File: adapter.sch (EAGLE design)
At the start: 28 parts, among them Q1 BS170, Q2 BS170, Q3 BS170, Q4 BS170, X2 KUSBVX

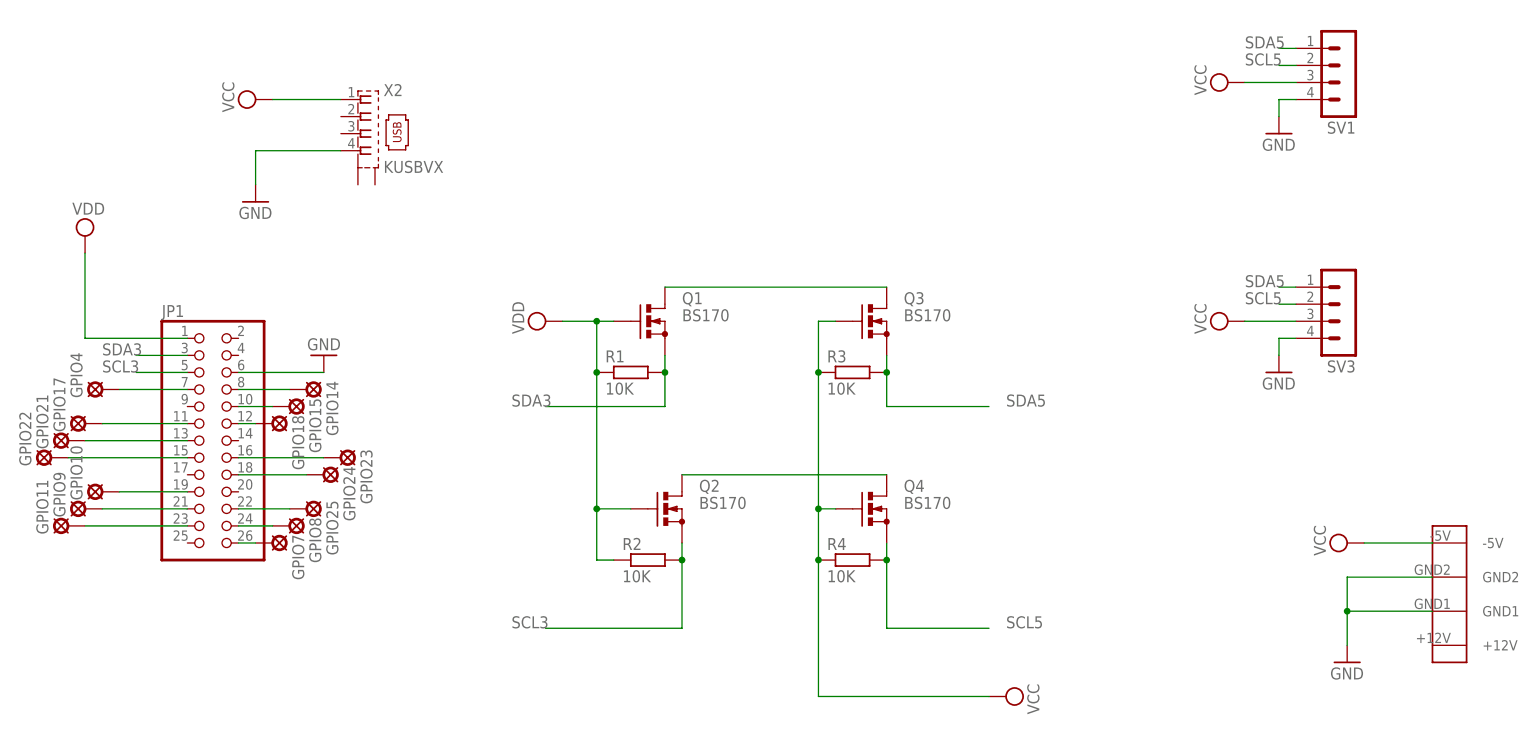
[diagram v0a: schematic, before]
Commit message: Redesign (INT-Leitung und breitere Leitung für Spannungsversorgung)
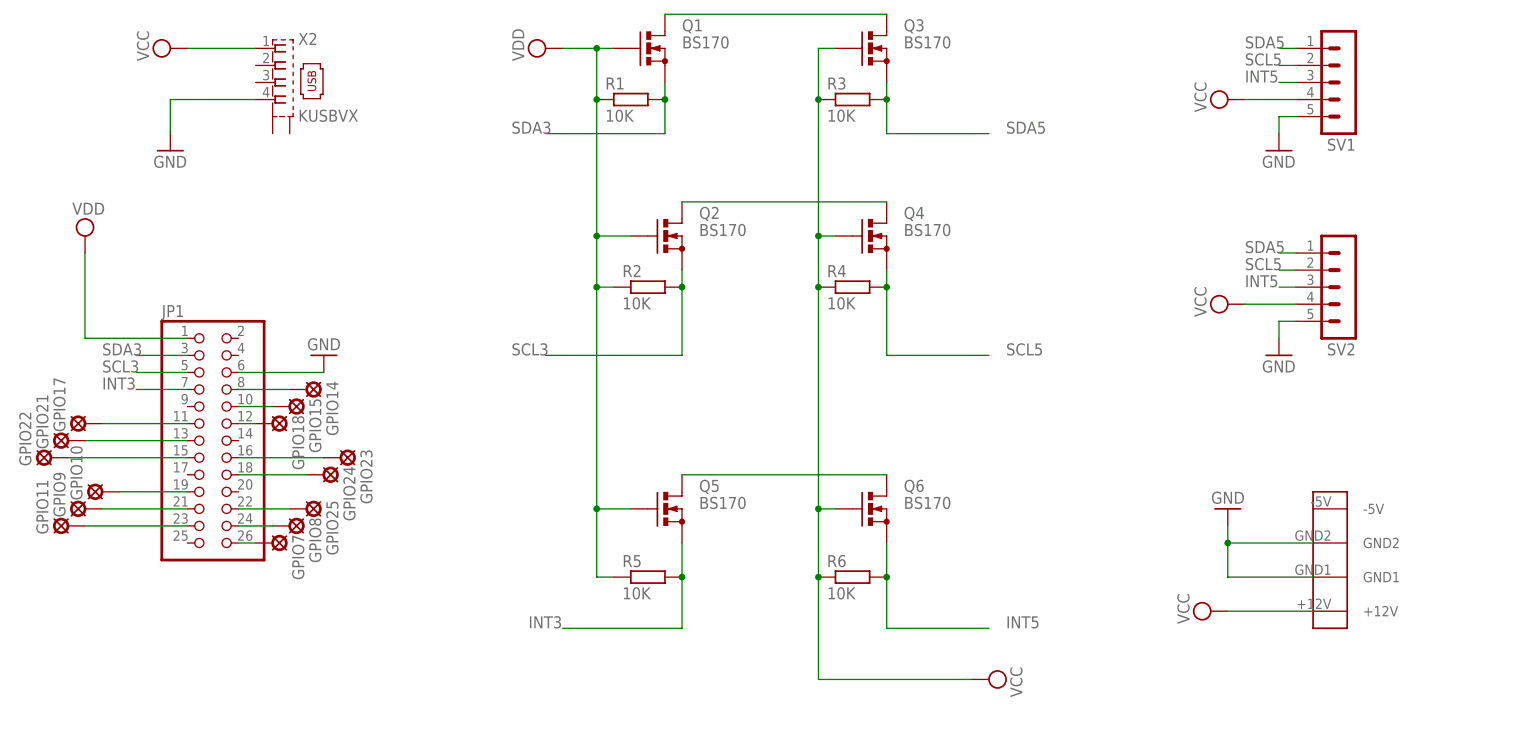
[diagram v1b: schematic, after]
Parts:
- removed GPIO4: LSP10, solpad:LSP10
- removed SV3: (no value), con-lstb:MA04-1
- added Q5, Q6: BS170, transistor-small-signal:BS170
- added R5, R6: 10K, resistor:R-EU_0207/2V
- added SV2: (no value), con-lstb:MA05-1
- R1, R2, R3, R4: device resistor:R-EU_0207/10 -> resistor:R-EU_0207/2V
- SV1: device con-lstb:MA04-1 -> con-lstb:MA05-1
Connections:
- removed net GPIO4: GPIO4.MP, JP1.7
- new net INT3: JP1.7, Q5.S, R5.2
- new net INT5: Q6.S, R6.2, SV1.3, SV2.3
- new net N$17: Q5.D, Q6.D
- net GND: now also SV1.5, SV2.5; no longer SV1.4, SV3.4
- net SCL5: now also SV2.2; no longer SV3.2
- net SDA5: now also SV2.1; no longer SV3.1
- net VCC: now also Q6.G, R6.1, SV1.4, SV2.4, U$1.+12V; no longer SV1.3, SV3.3, U$1.-5V
- net VDD: now also Q5.G, R5.1
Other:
- moved on the sheet: Q1, Q2, Q3, Q4, R1, R2, R3, R4, X2

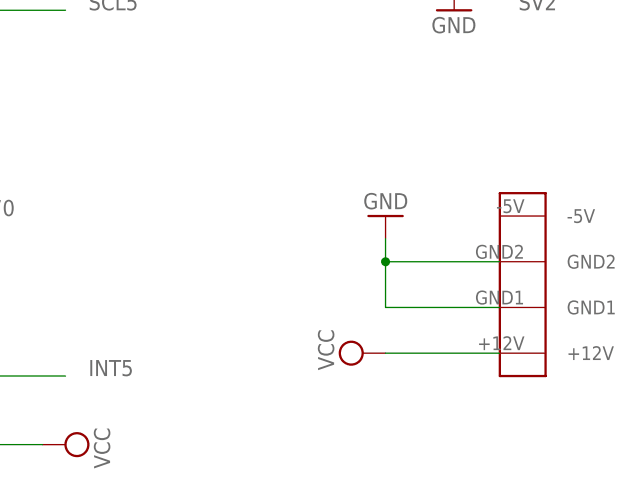
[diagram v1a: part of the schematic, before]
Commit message: Adapter: stecker angepasst Controller: board redesign
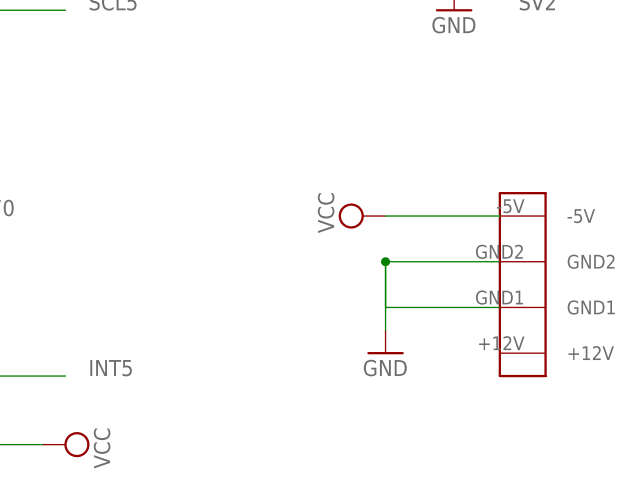
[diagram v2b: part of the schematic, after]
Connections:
- net VCC: now also U$1.-5V; no longer U$1.+12V
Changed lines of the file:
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@@
 <instance part="SUPPLY4" gate="G$1" x="116.84" y="53.34" rot="R90"/>
 <instance part="GND2" gate="1" x="124.46" y="45.72"/>
-<instance part="GND4" gate="1" x="116.84" y="-7.62" rot="R180"/>
-<instance part="SUPPLY6" gate="G$1" x="114.3" y="-22.86" rot="R90"/>
+<instance part="GND4" gate="1" x="116.84" y="-22.86"/>
+<instance part="SUPPLY6" gate="G$1" x="114.3" y="-7.62" rot="R90"/>
 <instance part="U$1" gate="G$1" x="129.54" y="-15.24" rot="R90"/>
 <instance part="SV2" gate="G$1" x="134.62" y="25.4" rot="R180"/>
@@
 <segment>
 <pinref part="SUPPLY6" gate="G$1" pin="VCC"/>
-<pinref part="U$1" gate="G$1" pin="+12V"/>
-<wire x1="116.84" y1="-22.86" x2="129.54" y2="-22.86" width="0.1524" layer="91"/>
+<pinref part="U$1" gate="G$1" pin="-5V"/>
+<wire x1="116.84" y1="-7.62" x2="129.54" y2="-7.62" width="0.1524" layer="91"/>
 </segment>
 </net>
@@
 <wire x1="116.84" y1="-12.7" x2="129.54" y2="-12.7" width="0.1524" layer="91"/>
 <pinref part="GND4" gate="1" pin="GND"/>
-<wire x1="116.84" y1="-10.16" x2="116.84" y2="-12.7" width="0.1524" layer="91"/>
+<wire x1="116.84" y1="-20.32" x2="116.84" y2="-12.7" width="0.1524" layer="91"/>
 <pinref part="U$1" gate="G$1" pin="GND1"/>
 <wire x1="129.54" y1="-17.78" x2="116.84" y2="-17.78" width="0.1524" layer="91"/>
